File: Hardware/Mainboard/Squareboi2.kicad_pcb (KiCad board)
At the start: 2 copper layers, 72 x 139 mm, 32 parts, among them J1 GB-CART, J10 TP_CLK, J11 TP_40, J2 ROMC_L, J4 ROMC_C, J5 RAMC_L, J6 RAMC_R, J7 JTAG, J8 AUX_POW, SW1 SW_DIP_x02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

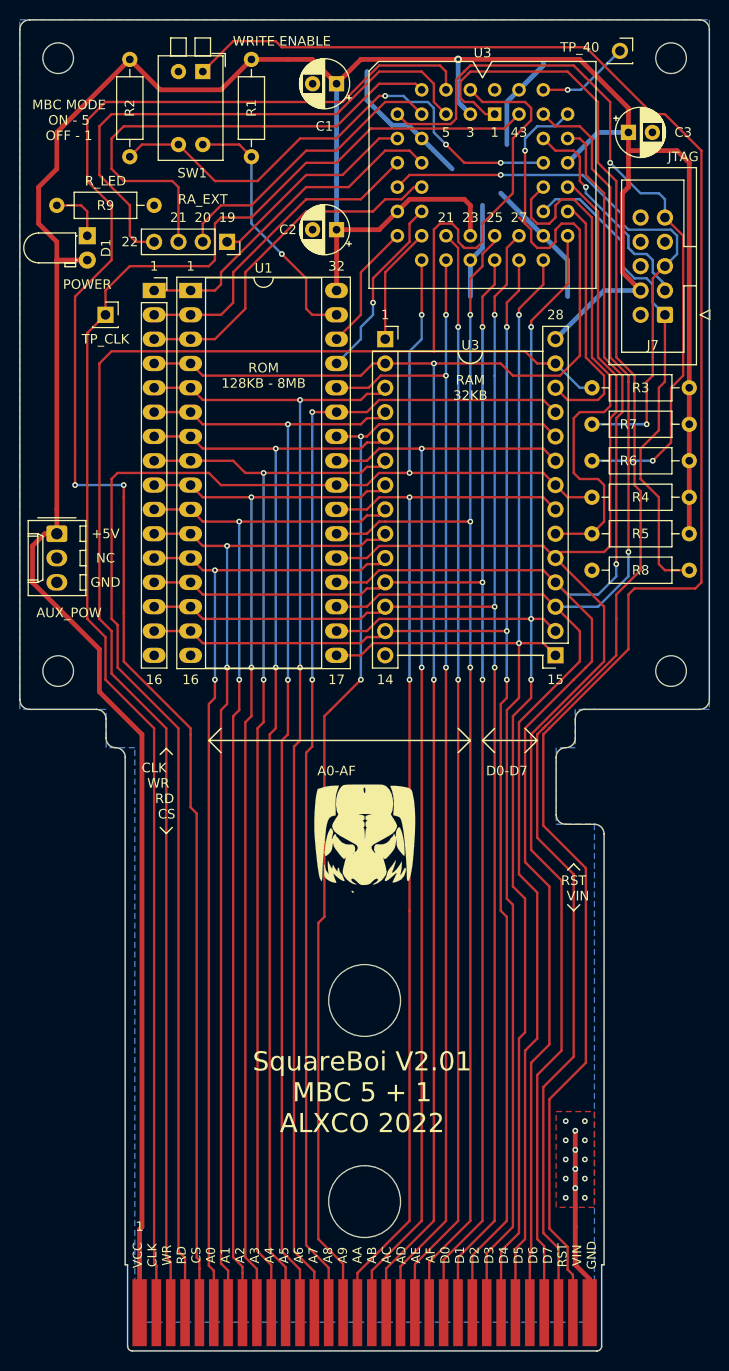
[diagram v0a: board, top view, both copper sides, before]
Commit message: Refactor pullup resistors
Add pullup to reset line for DMG compatibility, remove TDI and TMS pullups. Update mainboard to V2.02.
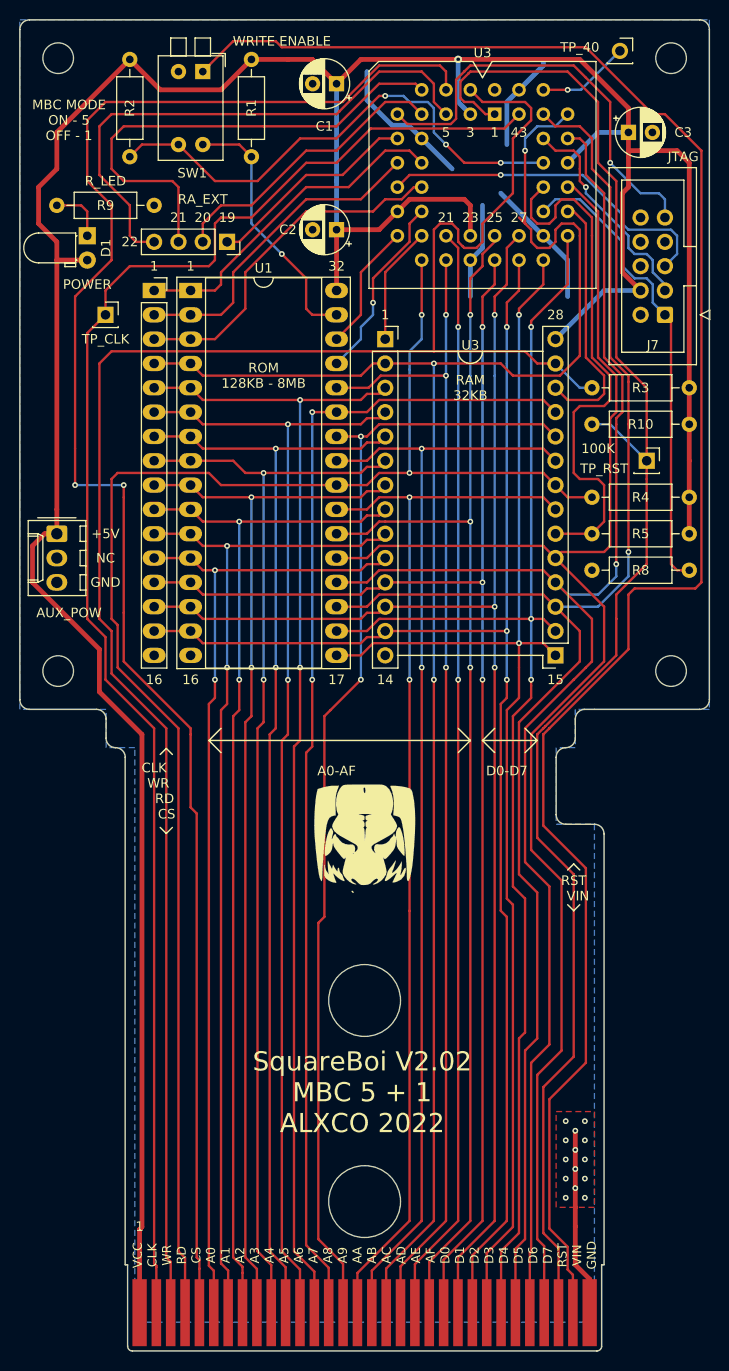
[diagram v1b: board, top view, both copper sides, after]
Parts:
- removed R6, R7: 20K, Resistor_THT:R_Axial_DIN0207_L6.3mm_D2.5mm_P10.16mm_Horizontal
- added J12: TP_RST, Connector_PinSocket_2.54mm:PinSocket_1x01_P2.54mm_Vertical, F.Cu at (84.5, 66.0)
- added R10: 100K, Resistor_THT:R_Axial_DIN0207_L6.3mm_D2.5mm_P10.16mm_Horizontal, F.Cu at (88.9, 62.2)
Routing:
- net /TDI: track 78.6 -> 44.7 mm, vias 2 -> 1
- net /TMS: track 59.6 -> 36.6 mm, vias 2 -> 1
- net /RS_N: track 158.4 -> 166.2 mm
- net /TCK: track 52.1 -> 49.3 mm
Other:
- board text added: "SquareBoi V2.02 MBC 5 + 1 ALXCO 2022"
- board text removed: "SquareBoi V2.01 MBC 5 + 1 ALXCO 2022"

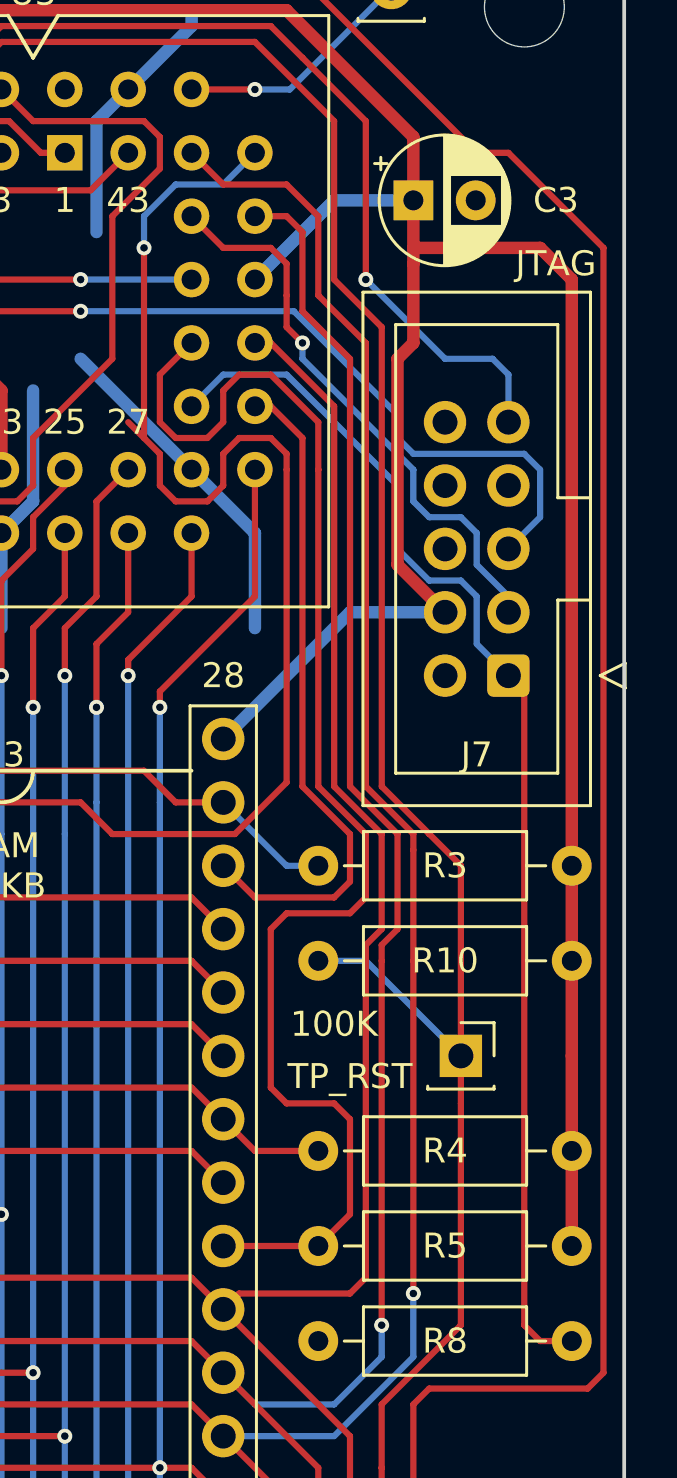
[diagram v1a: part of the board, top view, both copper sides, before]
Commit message: Remove reset pullup from Mainboard
Remove the RS_N pullup resistor after fixing pin keeper issue in software. Repackage corresponding gerbers.
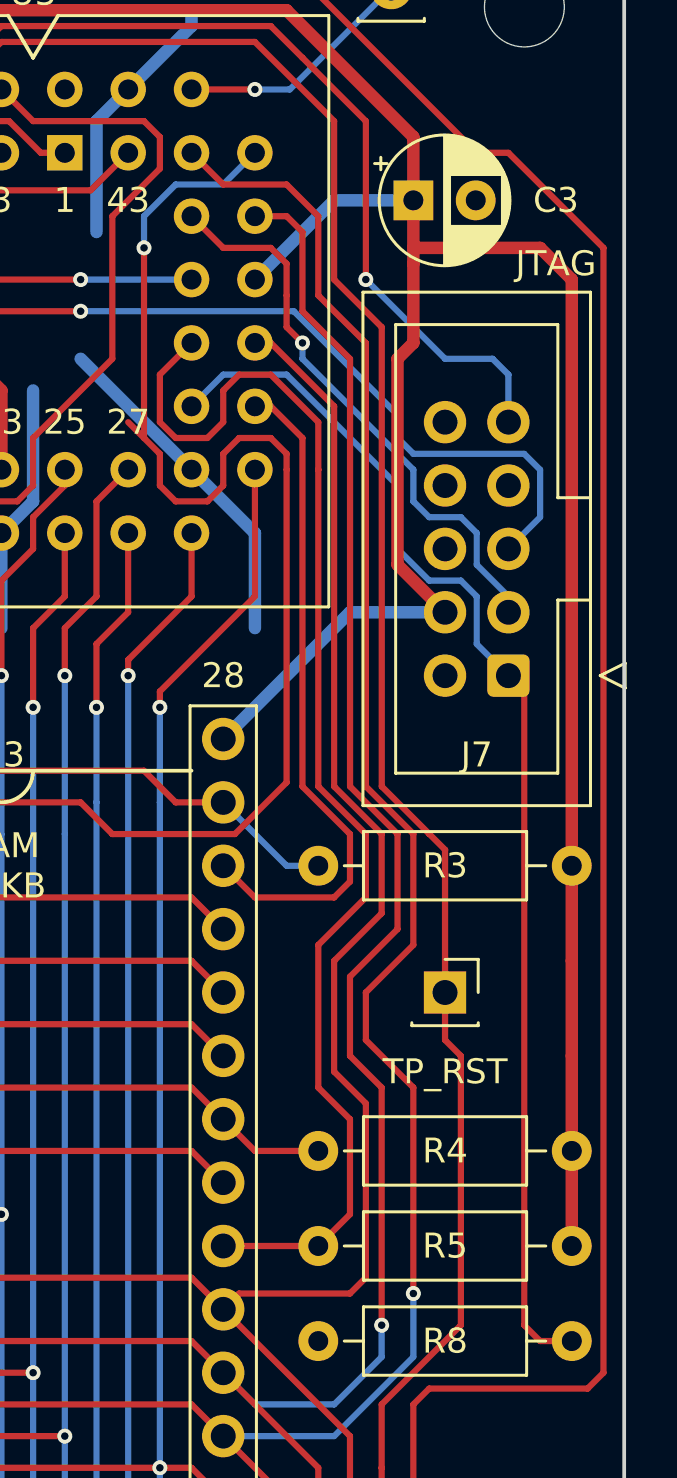
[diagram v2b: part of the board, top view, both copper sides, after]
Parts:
- removed R10: 100K, Resistor_THT:R_Axial_DIN0207_L6.3mm_D2.5mm_P10.16mm_Horizontal
- moved J12 2.62 mm to (83.8, 63.5)
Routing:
- net /RS_N: track 166.2 -> 158.9 mm
- net /RAMCS_N: track 56.5 -> 52.4 mm
- net /D5: track 165.4 -> 167.0 mm
- net /D6: track 163.3 -> 164.4 mm
- net /D7: track 157.1 -> 158.1 mm

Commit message: Update schematic capacitors
Move capacitor symbols to be closer to devices they're decoupling, fix value typo (10nf to 100nf)
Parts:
- C1, C2, C3: value 10nF -> 100n
